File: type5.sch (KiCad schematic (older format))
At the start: 3 parts, among them P1 CONN_01X09, P2 CONN_01X26, U1 TEENSYPP2

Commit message: mod
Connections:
- net at U1.1 (GND): now also P2.4 (P4)
- net at U1.47 (PB2): no longer P2.4 (P4)
- no-connect marks 19 -> 18
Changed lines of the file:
@@
 	5550 5700 5550 6050
-Wire Wire Line
-	5650 6050 5650 5750
-Wire Wire Line
-	5650 5750 6500 5750
-Wire Wire Line
-	6500 5750 6500 3200
-Wire Wire Line
-	6500 3200 5850 3200
 Wire Wire Line
 	5850 3100 6550 3100
@@
 NoConn ~ 4350 5100
 NoConn ~ 4250 5100
-NoConn ~ 3150 2700
 Wire Wire Line
 	2300 2800 3150 2800
@@
 Wire Wire Line
 	2300 3600 3150 3600
+Wire Wire Line
+	5650 6650 5650 6050
+Wire Wire Line
+	1650 6650 5650 6650
+Wire Wire Line
+	1650 6650 1650 2700
+Wire Wire Line
+	1650 2700 3150 2700
 $EndSCHEMATC

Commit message: asd
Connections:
- net at U1.1 (GND): now also P2.23 (P23); no longer P2.4 (P4)
- net at U1.14 (PC1): no longer P2.23 (P23)
- net at U1.47 (PB2): now also P2.4 (P4)
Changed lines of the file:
@@
 	3850 5500 3850 6050
-Wire Wire Line
-	3750 6050 3750 5550
-Wire Wire Line
-	3750 5550 2850 5550
-Wire Wire Line
-	2850 5550 2850 4000
-Wire Wire Line
-	2850 4000 3150 4000
 Wire Wire Line
 	3150 3900 2800 3900
@@
 	2300 3600 3150 3600
 Wire Wire Line
-	5650 6650 5650 6050
+	5650 6050 5650 5750
 Wire Wire Line
-	1650 6650 5650 6650
+	5650 5750 6500 5750
 Wire Wire Line
-	1650 6650 1650 2700
+	6500 5750 6500 3200
 Wire Wire Line
-	1650 2700 3150 2700
+	6500 3200 5850 3200
+Wire Wire Line
+	3750 6050 3750 6450
+Wire Wire Line
+	3750 6450 1750 6450
+Wire Wire Line
+	1750 6450 1750 2700
+Wire Wire Line
+	1750 2700 3150 2700
 $EndSCHEMATC

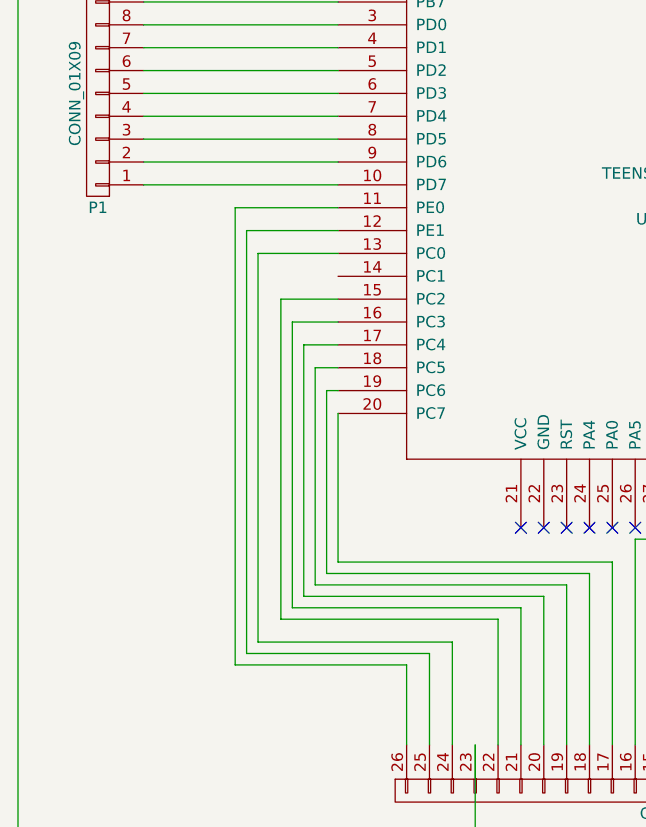
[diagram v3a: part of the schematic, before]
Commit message: fix, d6 unused
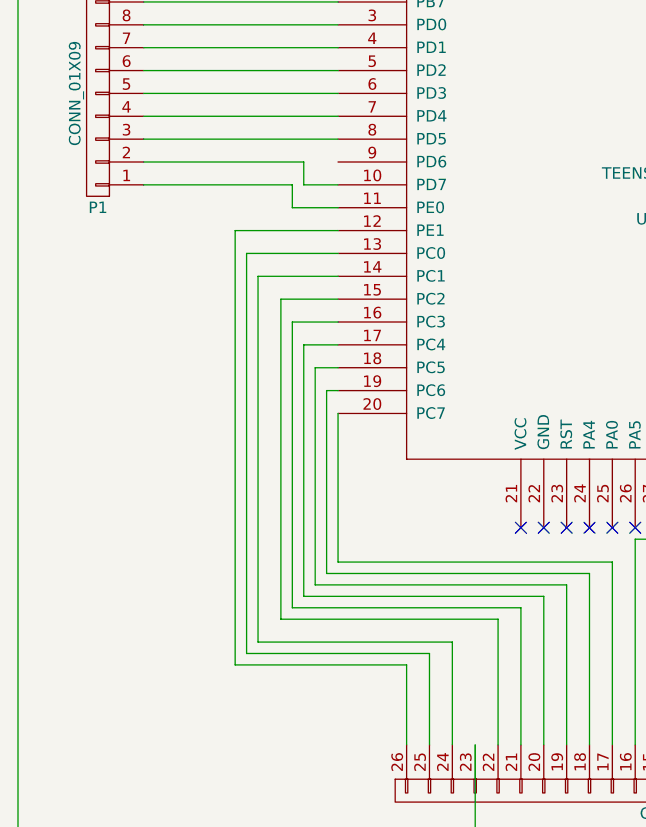
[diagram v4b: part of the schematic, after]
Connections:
- net at U1.10 (PD7): now also P1.2 (P2); no longer P1.1 (P1)
- net at U1.11 (PE0): now also P1.1 (P1); no longer P2.26 (P26)
- net at U1.12 (PE1): now also P2.26 (P26); no longer P2.25 (P25)
- net at U1.13 (PC0): now also P2.25 (P25); no longer P2.24 (P24)
- net at U1.14 (PC1): now also P2.24 (P24)
- net at U1.9 (PD6): no longer P1.2 (P2)
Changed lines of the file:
@@
 	3850 5500 3850 6050
-Wire Wire Line
-	3150 3900 2800 3900
-Wire Wire Line
-	2800 3900 2800 5600
 Wire Wire Line
 	2800 5600 3650 5600
@@
 Wire Wire Line
 	3550 5650 2750 5650
-Wire Wire Line
-	2750 5650 2750 3800
-Wire Wire Line
-	2750 3800 3150 3800
-Wire Wire Line
-	3150 3700 2700 3700
-Wire Wire Line
-	2700 3700 2700 5700
 Wire Wire Line
 	2700 5700 3450 5700
@@
 	2300 3400 3150 3400
 Wire Wire Line
-	3150 3500 2300 3500
-Wire Wire Line
-	2300 3600 3150 3600
-Wire Wire Line
 	5650 6050 5650 5750
 Wire Wire Line
@@
 Wire Wire Line
 	1750 2700 3150 2700
+Wire Wire Line
+	3150 4000 2800 4000
+Wire Wire Line
+	2800 4000 2800 5600
+Wire Wire Line
+	2750 5650 2750 3900
+Wire Wire Line
+	2750 3900 3150 3900
+Wire Wire Line
+	3150 3800 2700 3800
+Wire Wire Line
+	2700 3800 2700 5700
+Wire Wire Line
+	2300 3500 3000 3500
+Wire Wire Line
+	3000 3500 3000 3600
+Wire Wire Line
+	3000 3600 3150 3600
+Wire Wire Line
+	3150 3700 2950 3700
+Wire Wire Line
+	2950 3700 2950 3600
+Wire Wire Line
+	2950 3600 2300 3600
 $EndSCHEMATC

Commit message: finish (hope)
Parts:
- added R1: R, Resistors_ThroughHole:Resistor_Horizontal_RM7mm, symbol R
- P1: footprint myfootprint:ffc_1.25mm_9p -> myfootprint:ffc_1.25mm_9p_oval
- P2: footprint myfootprint:ffc_1.25m_26p -> myfootprint:ffc_1.25m_26p_oval
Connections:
- net at U1.1 (GND): no longer P2.23 (P23)
- net at U1.52 (VCC): now also R1.1
- new net: P2.23 (P23), R1.2
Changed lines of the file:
@@
 F 0 "P2" H 4700 7600 50  0000 C CNN
 F 1 "CONN_01X26" V 4800 6250 50  0000 C CNN
-F 2 "myfootprint:ffc_1.25m_26p" H 4700 6250 50  0001 C CNN
+F 2 "myfootprint:ffc_1.25m_26p_oval" H 4700 6250 50  0001 C CNN
 F 3 "" H 4700 6250 50  0000 C CNN
 	1    4700 6250
 	0    1    1    0
 $EndComp
-NoConn ~ 5850 2700
 NoConn ~ 5850 3700
 NoConn ~ 5850 3800
@@
 F 0 "P1" H 2100 3700 50  0000 C CNN
 F 1 "CONN_01X09" V 2200 3200 50  0000 C CNN
-F 2 "myfootprint:ffc_1.25mm_9p" H 2100 3200 50  0001 C CNN
+F 2 "myfootprint:ffc_1.25mm_9p_oval" H 2100 3200 50  0001 C CNN
 F 3 "" H 2100 3200 50  0000 C CNN
 	1    2100 3200
@@
 	3750 6050 3750 6450
 Wire Wire Line
-	3750 6450 1750 6450
-Wire Wire Line
-	1750 6450 1750 2700
-Wire Wire Line
-	1750 2700 3150 2700
-Wire Wire Line
 	3150 4000 2800 4000
 Wire Wire Line
@@
 Wire Wire Line
 	2950 3600 2300 3600
+NoConn ~ 3150 2700
+Wire Wire Line
+	5850 2700 6800 2700
+Wire Wire Line
+	6800 2700 6800 6450
+$Comp
+L R R1
+U 1 1 57319DE9
+P 6650 6450
+F 0 "R1" V 6730 6450 50  0000 C CNN
+F 1 "R" V 6650 6450 50  0000 C CNN
+F 2 "Resistors_ThroughHole:Resistor_Horizontal_RM7mm" V 6580 6450 50  0001 C CNN
+F 3 "" H 6650 6450 50  0000 C CNN
+	1    6650 6450
+	0    1    1    0
+$EndComp
+Wire Wire Line
+	3750 6450 6500 6450
 $EndSCHEMATC
